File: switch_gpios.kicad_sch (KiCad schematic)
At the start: 16 parts

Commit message: connects SPI from STM to Switch. Refs: #1
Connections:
- net SPI_SLV.CLK renamed SPI_STM_SWITCH.CLK
- net SPI_SLV.DI renamed SPI_STM_SWITCH.MOSI
- net SPI_SLV.DO renamed SPI_STM_SWITCH.MISO
- net SPI_SLV.nCS renamed SPI_STM_SWITCH.nCS

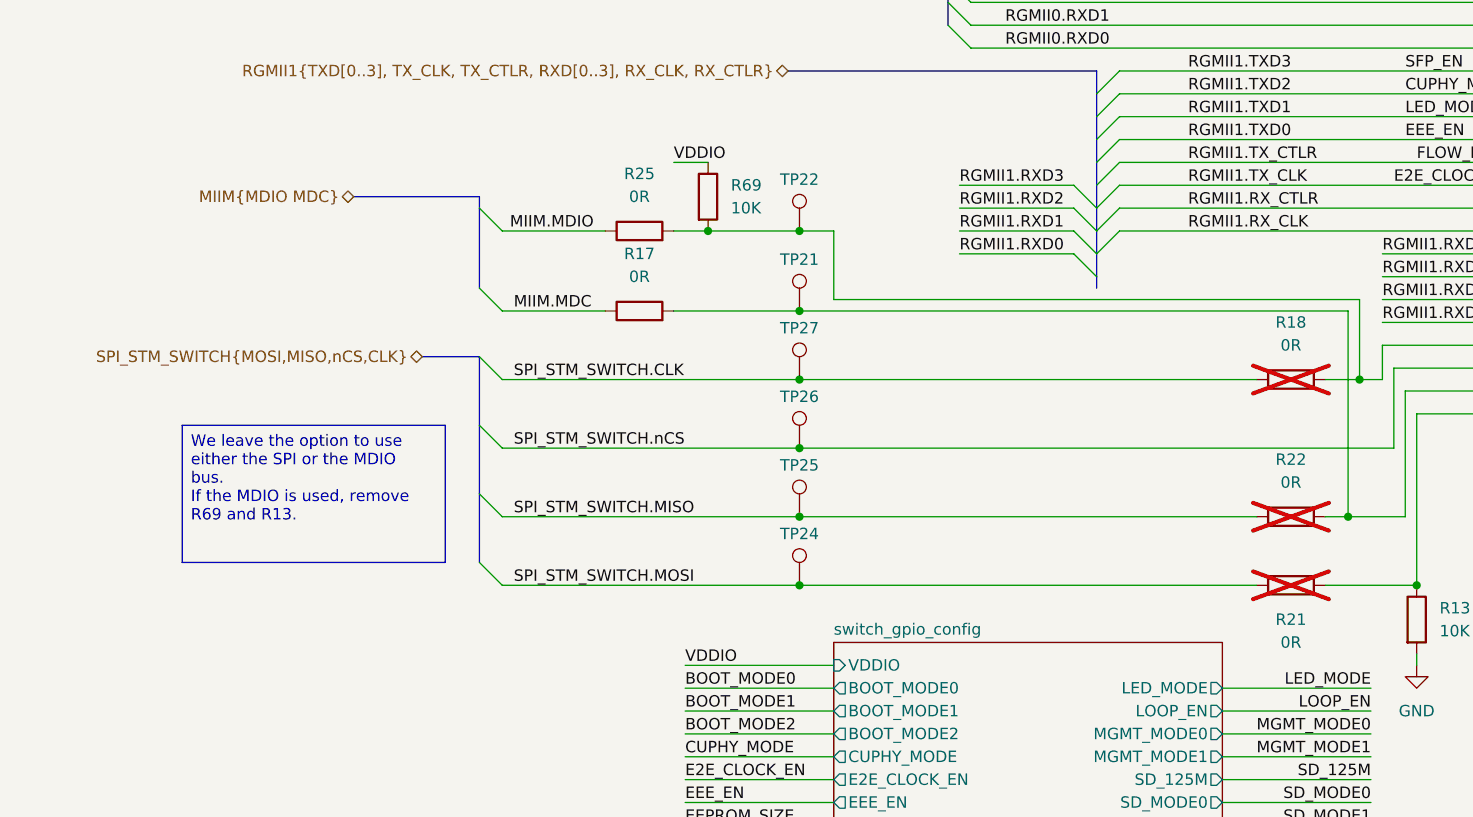
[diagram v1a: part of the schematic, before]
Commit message: connects MIIM bus from STM to Switch. Refs: #1
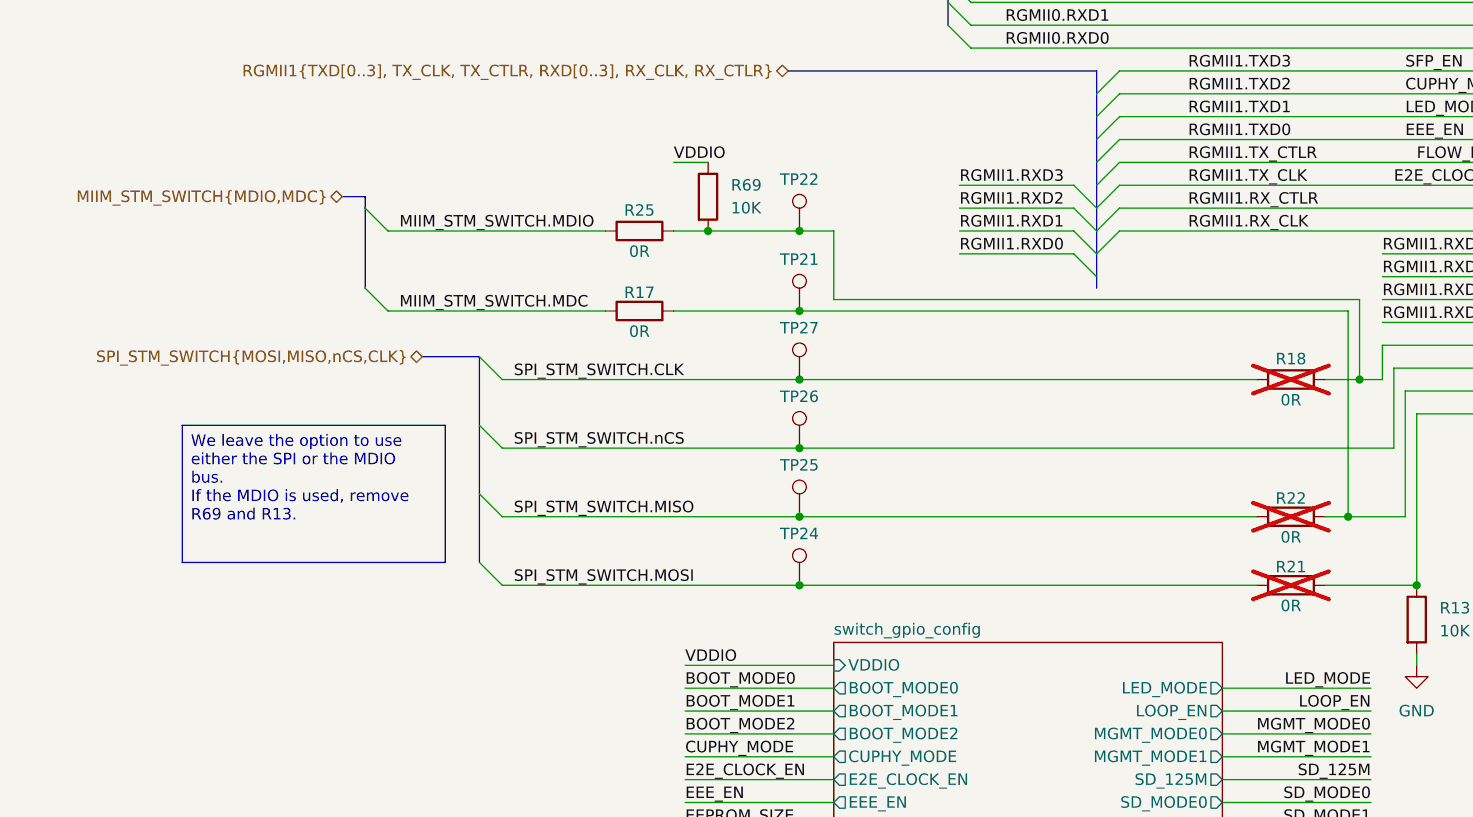
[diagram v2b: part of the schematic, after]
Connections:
- net MIIM.MDC renamed MIIM_STM_SWITCH.MDC
- net MIIM.MDIO renamed MIIM_STM_SWITCH.MDIO
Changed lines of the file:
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@@
 	)
 	(bus_entry
+		(at 48.26 113.03)
+		(size 2.54 2.54)
+		(stroke
+			(width 0)
+			(type default)
+		)
+	)
+	(bus_entry
 		(at 129.54 105.41)
 		(size 2.54 -2.54)
@@
 	)
 	(bus_entry
-		(at 60.96 121.92)
-		(size 2.54 2.54)
-		(stroke
-			(width 0)
-			(type default)
-		)
-	)
-	(bus_entry
-		(at 60.96 113.03)
+		(at 48.26 121.92)
 		(size 2.54 2.54)
 		(stroke
@@
 	(wire
 		(pts
-			(xy 100.33 123.19) (xy 158.75 123.19)
+			(xy 50.8 115.57) (xy 74.93 115.57)
 		)
 		(stroke
@@
 		)
 	)
-	(bus
+	(wire
 		(pts
-			(xy 113.03 72.39) (xy 113.03 74.93)
+			(xy 100.33 123.19) (xy 158.75 123.19)
 		)
 		(stroke
@@
 		)
 	)
-	(wire
+	(bus
 		(pts
-			(xy 63.5 124.46) (xy 74.93 124.46)
+			(xy 113.03 72.39) (xy 113.03 74.93)
 		)
 		(stroke
@@
 	(bus
 		(pts
-			(xy 46.99 111.76) (xy 60.96 111.76)
+			(xy 45.72 111.76) (xy 48.26 111.76)
 		)
 		(stroke
@@
 	(bus
 		(pts
+			(xy 48.26 113.03) (xy 48.26 121.92)
+		)
+		(stroke
+			(width 0)
+			(type default)
+		)
+	)
+	(bus
+		(pts
 			(xy 60.96 137.16) (xy 60.96 144.78)
 		)
@@
 	(wire
 		(pts
-			(xy 63.5 115.57) (xy 74.93 115.57)
-		)
-		(stroke
-			(width 0)
-			(type default)
-		)
-	)
-	(wire
-		(pts
 			(xy 86.36 115.57) (xy 96.52 115.57)
 		)
@@
 	(bus
 		(pts
-			(xy 60.96 113.03) (xy 60.96 121.92)
+			(xy 48.26 111.76) (xy 48.26 113.03)
 		)
 		(stroke
@@
 	(wire
 		(pts
+			(xy 50.8 124.46) (xy 74.93 124.46)
+		)
+		(stroke
+			(width 0)
+			(type default)
+		)
+	)
+	(wire
+		(pts
 			(xy 154.94 147.32) (xy 157.48 147.32)
 		)
@@
 		)
 	)
-	(bus
-		(pts
-			(xy 60.96 111.76) (xy 60.96 113.03)
-		)
-		(stroke
-			(width 0)
-			(type default)
-		)
-	)
 	(wire
 		(pts
@@
 		)
 	)
+	(label "MIIM_STM_SWITCH.MDIO"
+		(at 52.07 115.57 0)
+		(effects
+			(font
+				(size 1.27 1.27)
+			)
+			(justify left bottom)
+		)
+	)
 	(label "SD_125M"
 		(at 163.83 77.47 0)
@@
 		)
 	)
-	(label "MIIM.MDIO"
-		(at 73.66 115.57 180)
+	(label "MIIM_STM_SWITCH.MDC"
+		(at 52.07 124.46 0)
 		(effects
 			(font
 				(size 1.27 1.27)
 			)
-			(justify right bottom)
+			(justify left bottom)
 		)
 	)
@@
 		)
 	)
-	(label "MIIM.MDC"
-		(at 64.77 124.46 0)
-		(effects
-			(font
-				(size 1.27 1.27)
-			)
-			(justify left bottom)
-		)
-	)
 	(label "RGMII0.TXD2"
 		(at 119.38 69.85 0)
@@
 		)
 	)
-	(hierarchical_label "MIIM{MDIO MDC}"
+	(hierarchical_label "MIIM_STM_SWITCH{MDIO,MDC}"
 		(shape bidirectional)
-		(at 46.99 111.76 180)
+		(at 45.72 111.76 180)
 		(effects
 			(font
@@
 		(on_board yes)
 		(dnp no)
-		(fields_autoplaced yes)
 		(property "Reference" "R17"
-			(at 78.74 118.11 90)
+			(at 78.74 122.428 90)
 			(effects
 				(font
@@
 		)
 		(property "Value" "0R"
-			(at 78.74 120.65 90)
+			(at 78.74 126.746 90)
 			(effects
 				(font
@@
 		(on_board yes)
 		(dnp yes)
-		(fields_autoplaced yes)
 		(property "Reference" "R18"
-			(at 151.13 125.73 90)
+			(at 151.13 129.794 90)
 			(effects
 				(font
@@
 		)
 		(property "Value" "0R"
-			(at 151.13 128.27 90)
+			(at 151.13 134.366 90)
 			(effects
 				(font
@@
 		(on_board yes)
 		(dnp no)
-		(fields_autoplaced yes)
 		(property "Reference" "R25"
-			(at 78.74 109.22 90)
+			(at 78.74 113.284 90)
 			(effects
 				(font
@@
 		)
 		(property "Value" "0R"
-			(at 78.74 111.76 90)
+			(at 78.74 117.856 90)
 			(effects
 				(font
@@
 		(on_board yes)
 		(dnp yes)
-		(fields_autoplaced yes)
 		(property "Reference" "R22"
-			(at 151.13 140.97 90)
+			(at 151.13 145.288 90)
 			(effects
 				(font
@@
 		)
 		(property "Value" "0R"
-			(at 151.13 143.51 90)
+			(at 151.13 149.606 90)
 			(effects
 				(font
@@
 		(on_board yes)
 		(dnp yes)
-		(fields_autoplaced yes)
 		(property "Reference" "R21"
-			(at 151.13 158.75 90)
+			(at 151.13 152.908 90)
 			(effects
 				(font
@@
 		)
 		(property "Value" "0R"
-			(at 151.13 161.29 90)
+			(at 151.13 157.226 90)
 			(effects
 				(font

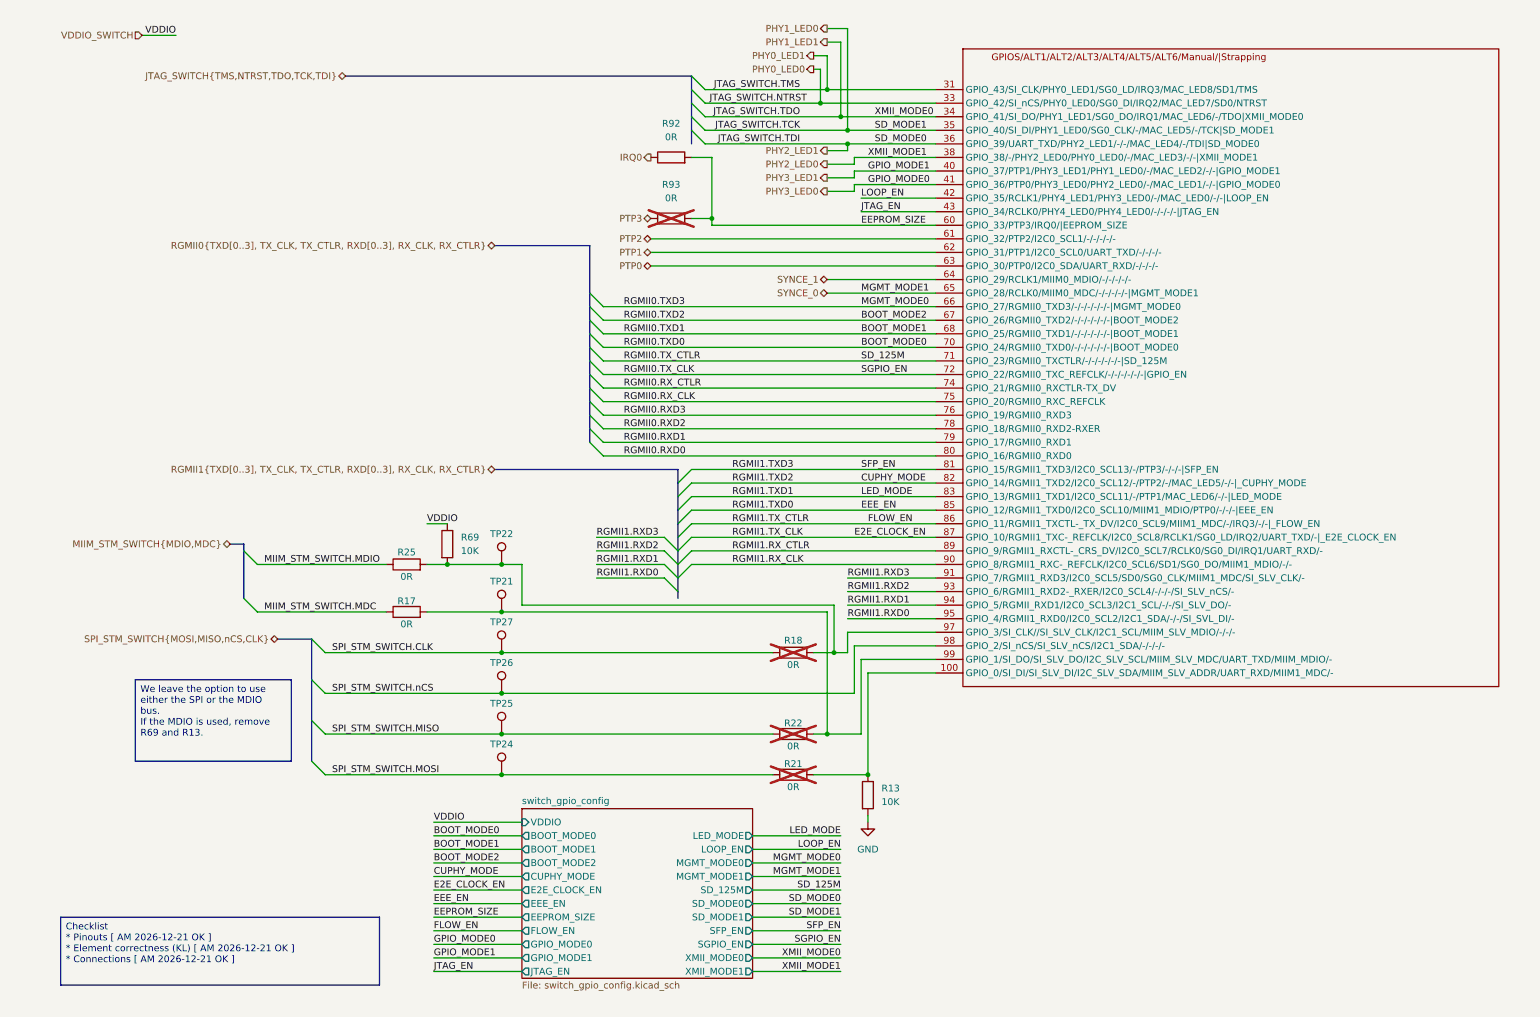
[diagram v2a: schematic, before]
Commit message: connects RGMII1 bus between Switch and STM. Refs: #1
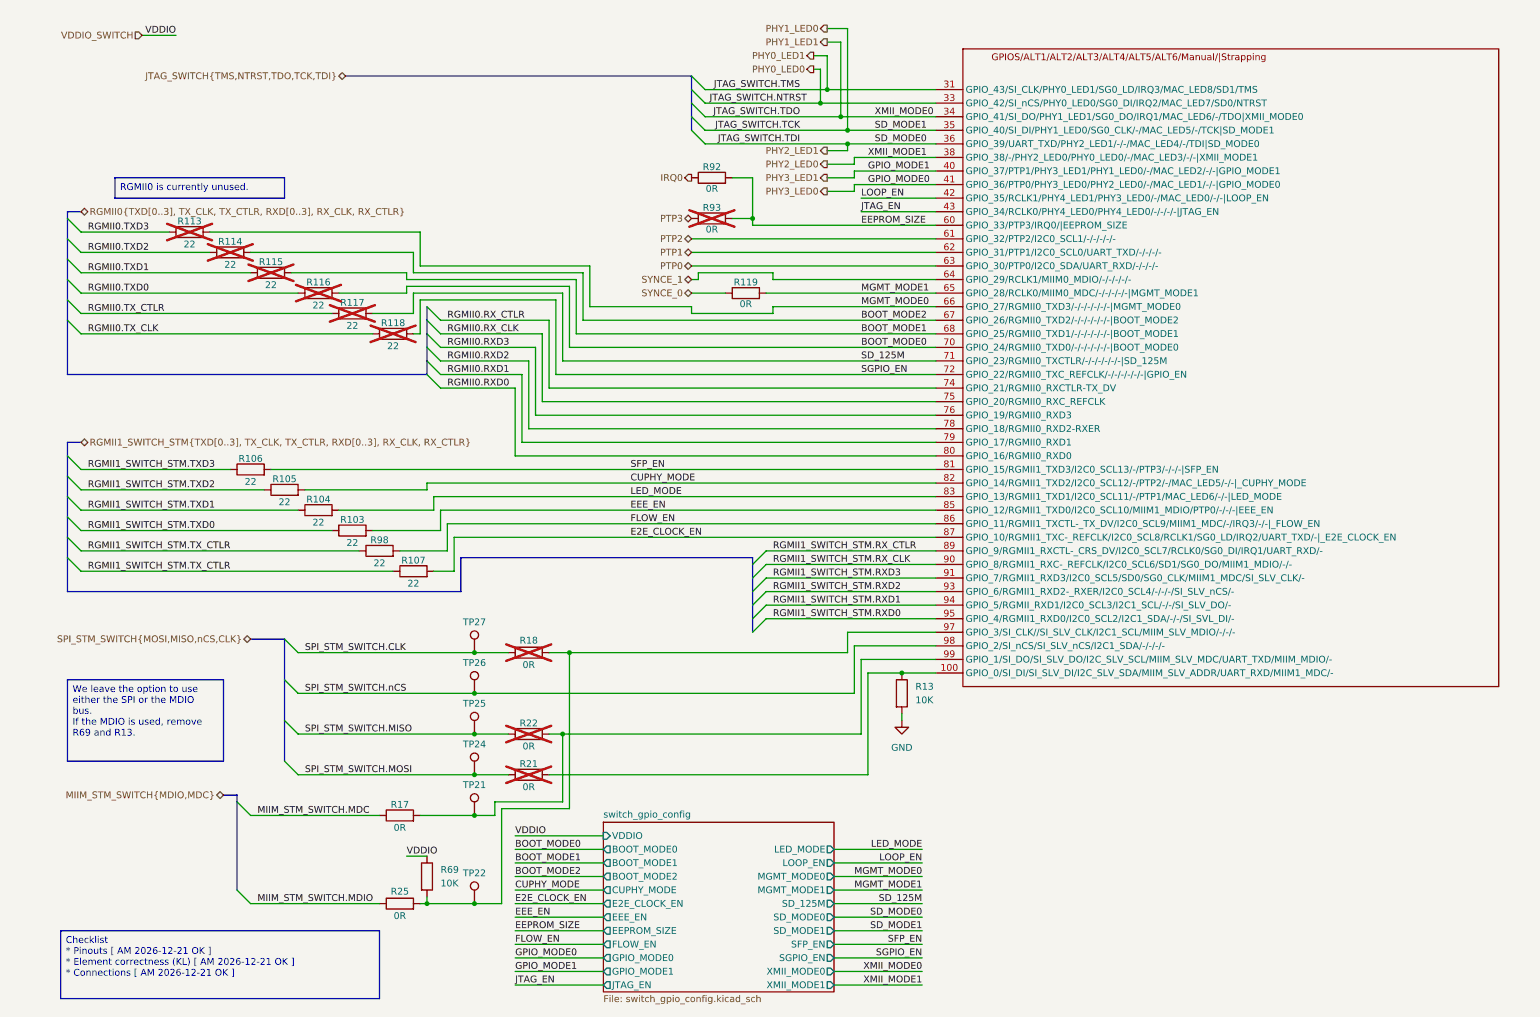
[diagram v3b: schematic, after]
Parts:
- added R103, R104, R105, R106, R107, R113, R114, R115, R116, R117, R118, R98: 22, KL_Footprints:R_0603, symbol KL_R:R_22_100mW_1pct_0603
- added R119: 0R, KL_Footprints:R_0603, symbol KL_R:R_0R_250mW_0.5_0603
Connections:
- net BOOT_MODE0: now also R116.2
- net BOOT_MODE1: now also R115.2
- net BOOT_MODE2: now also R114.2
- net CUPHY_MODE: now also R105.2
- net E2E_CLOCK_EN: now also R107.2
- net EEE_EN: now also R103.2
- net FLOW_EN: now also R98.2
- net LED_MODE: now also R104.2
- net MGMT_MODE0: now also R113.2
- net RGMII0.TX_CLK: now also R118.1; no longer U1.72 (GPIO_22/RGMII0_TXC_REFCLK/-/-/-/-/-/-|GPIO_EN)
- net RGMII0.TX_CTLR: now also R117.1; no longer U1.71 (GPIO_23/RGMII0_TXCTLR/-/-/-/-/-/-|SD_125M)
- net SYNCE_0: now also R119.1; no longer U1.65 (GPIO_28/RCLK0/MIIM0_MDC/-/-/-/-/-|MGMT_MODE1)
- net RGMII1.RXD0 renamed RGMII1_SWITCH_STM.RXD0
- net RGMII1.RXD1 renamed RGMII1_SWITCH_STM.RXD1
- net RGMII1.RXD2 renamed RGMII1_SWITCH_STM.RXD2
- net RGMII1.RXD3 renamed RGMII1_SWITCH_STM.RXD3
- net RGMII1.RX_CLK renamed RGMII1_SWITCH_STM.RX_CLK
- net RGMII1.RX_CTLR renamed RGMII1_SWITCH_STM.RX_CTLR
- net RGMII1.TXD3 renamed SFP_EN
- net SFP_EN: now also R106.2
- new net MGMT_MODE1: R119.2, U1.65 (GPIO_28/RCLK0/MIIM0_MDC/-/-/-/-/-|MGMT_MODE1)
- new net RGMII0.TXD0: R116.1
- new net RGMII0.TXD1: R115.1
- new net RGMII0.TXD2: R114.1
- new net RGMII0.TXD3: R113.1
- new net RGMII1_SWITCH_STM.TXD0: R103.1
- new net RGMII1_SWITCH_STM.TXD1: R104.1
- new net RGMII1_SWITCH_STM.TXD2: R105.1
- new net RGMII1_SWITCH_STM.TXD3: R106.1
- new net RGMII1_SWITCH_STM.TX_CTLR: R107.1, R98.1
- new net SD_125M: R117.2, U1.71 (GPIO_23/RGMII0_TXCTLR/-/-/-/-/-/-|SD_125M)
- new net SGPIO_EN: R118.2, U1.72 (GPIO_22/RGMII0_TXC_REFCLK/-/-/-/-/-/-|GPIO_EN)
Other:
- moved on the sheet: R13, R17, R18, R21, R22, R25, R69, R92, R93, TP21, TP22, TP24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

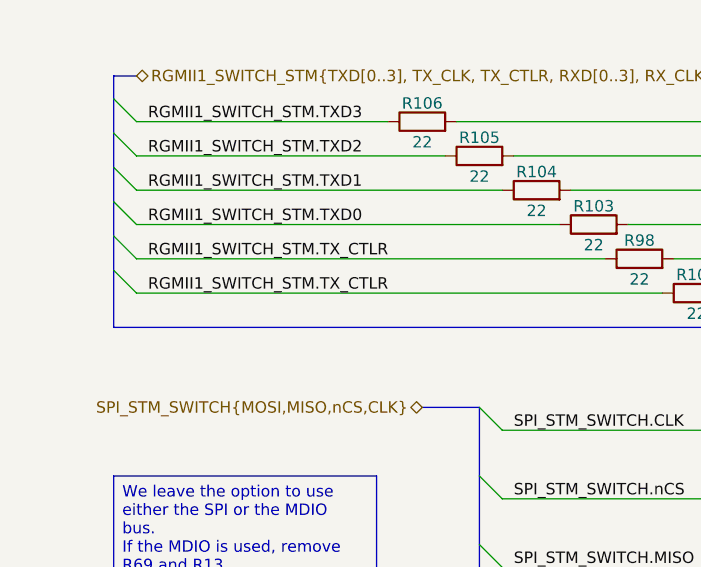
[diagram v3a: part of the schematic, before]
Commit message: fixes RGMII1 TX and RX resistors and duplicate name. Refs: #1
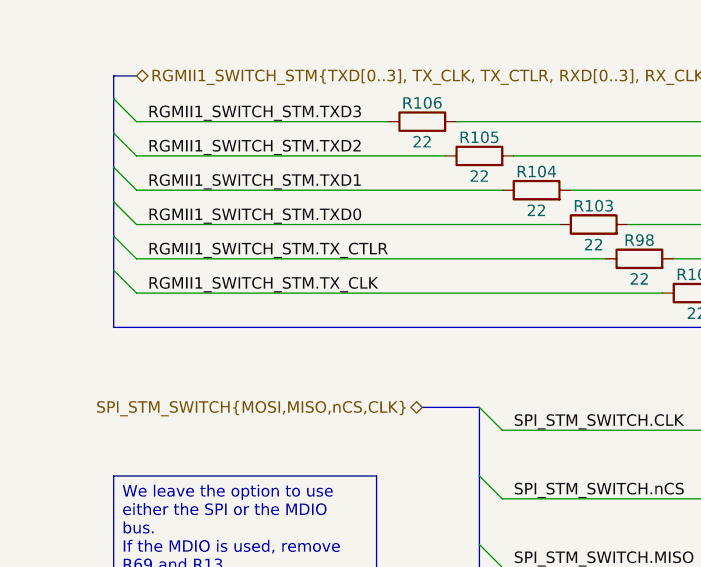
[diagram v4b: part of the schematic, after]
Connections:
- net RGMII1_SWITCH_STM.TX_CTLR: no longer R107.1
- new net RGMII1_SWITCH_STM.TX_CLK: R107.1
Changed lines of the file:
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@@
 		)
 	)
-	(label "RGMII1_SWITCH_STM.TX_CTLR"
+	(label "RGMII1_SWITCH_STM.TX_CLK"
 		(at 19.05 116.84 0)
 		(effects

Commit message: fixes ERC errors in DC/DC converters
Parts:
- R13, R69: footprint KL_Footprints:C_0603 -> KL_Footprints:R_0603
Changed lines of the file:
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@@
 			)
 		)
-		(property "Footprint" "KL_Footprints:C_0603"
+		(property "Footprint" "KL_Footprints:R_0603"
 			(at 80.772 173.99 90)
 			(effects
@@
 			)
 		)
-		(property "Footprint" "KL_Footprints:C_0603"
+		(property "Footprint" "KL_Footprints:R_0603"
 			(at 169.672 139.7 90)
 			(effects
